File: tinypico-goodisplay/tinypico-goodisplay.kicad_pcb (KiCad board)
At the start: 2 copper layers, 53.8 x 17.8 mm, 34 parts, among them J1 AFC24-S24FIC-00, Q1 Si1308, U1 TinypicoESP32_Symbol, U2 PCF8563T, Y1 Crystal_Small

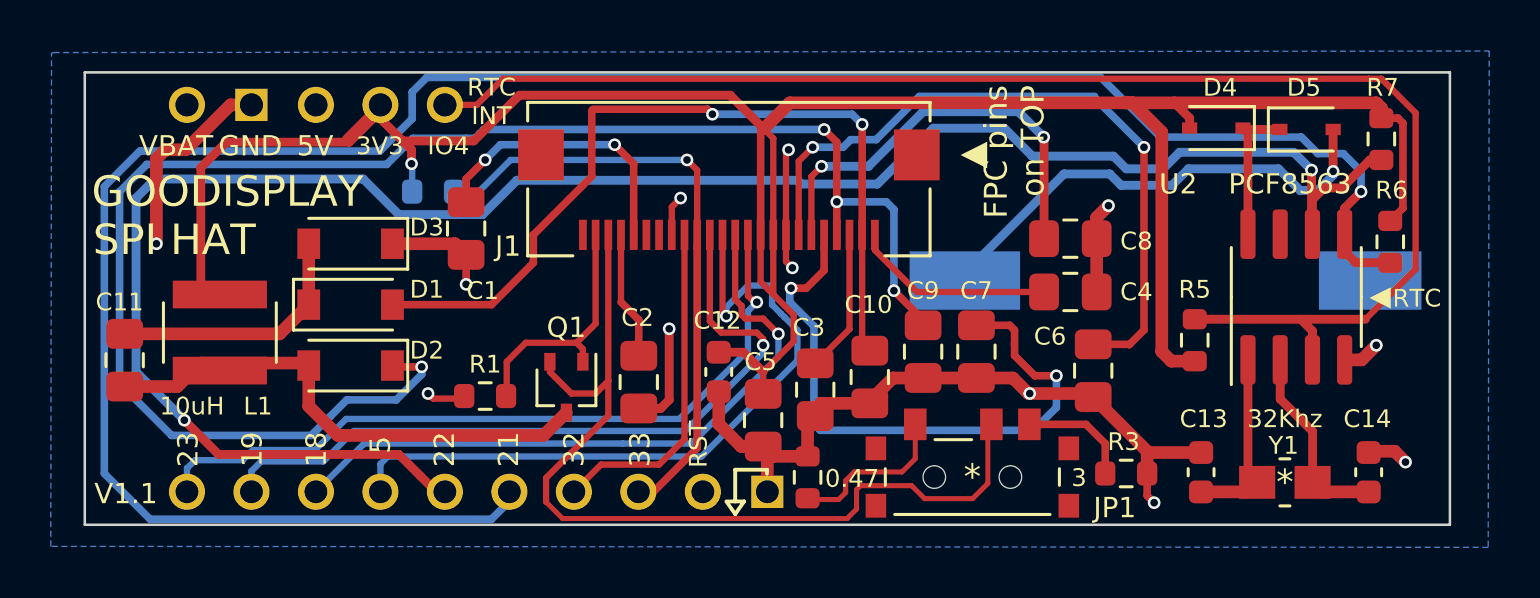
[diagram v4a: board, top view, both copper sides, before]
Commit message: Relabeling Sylkscreen with SPI pins
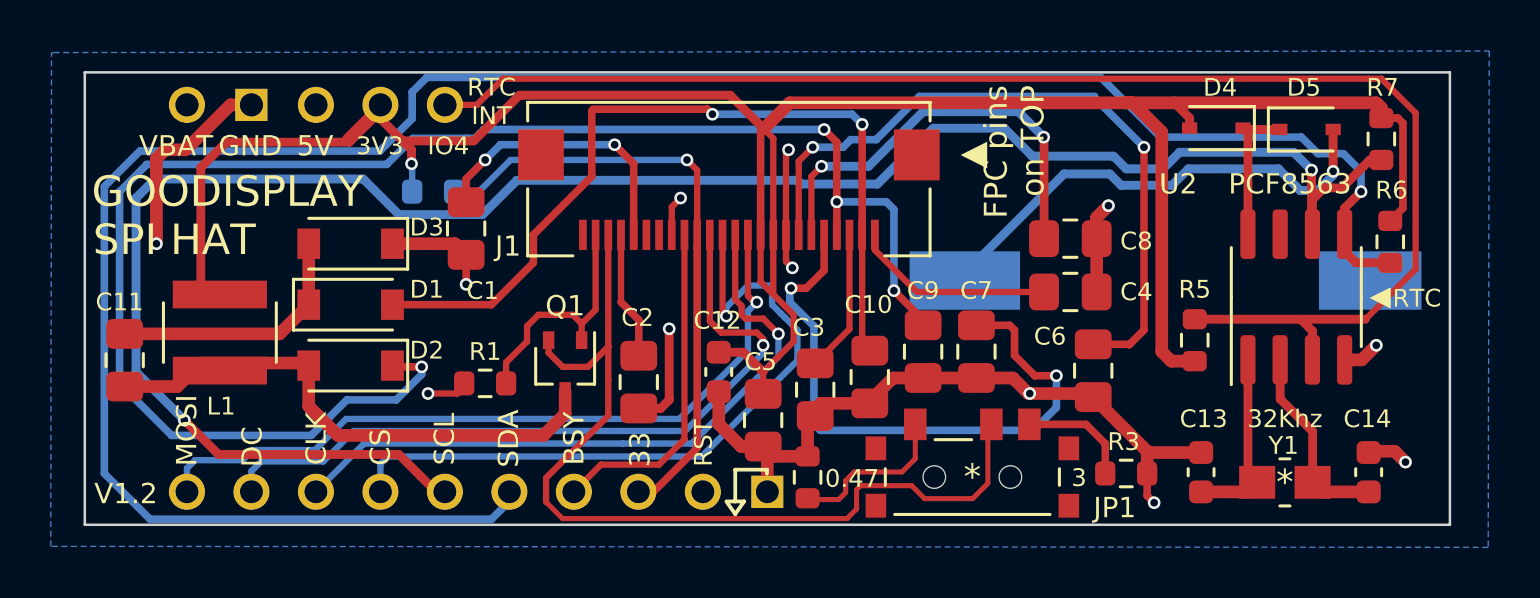
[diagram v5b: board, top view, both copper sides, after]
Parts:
- moved Q1 0.85 mm to (91.2, 46.4)
- moved R1 0.50 mm to (88.0, 47.0)
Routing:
- net Net-(C11-Pad2): track 20.3 -> 21.1 mm
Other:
- board text added: "BSY"
- board text added: "CLK"
- board text added: "CS"
- board text added: "DC"
- board text added: "MOSI"
- board text added: "SCL"
- board text added: "SDA"
- board text added: "V1.2"
- board text removed: "18"
- board text removed: "19"
- board text removed: "21"
- board text removed: "22"
- board text removed: "23"
- board text removed: "32"
- board text removed: "5"
- board text removed: "V1.1"
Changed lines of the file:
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@@
   )
   (footprint "Package_TO_SOT_SMD:SOT-323_SC-70" (layer "F.Cu")
-    (at 91.2 47.2 -90)
+    (at 91.15 46.35 -90)
     (descr "SOT-323, SC-70")
     (tags "SOT-323 SC-70")
@@
     (property "Sheetname" "")
     (attr through_hole)
-    (fp_text reference "L1" (at -2.9 1.5 180) (layer "F.SilkS")
-      (effects (font (size 0.7 0.7) (thickness 0.13)))
-    )
-    (fp_text value "10uH" (at -2.9 -1.1 180) (layer "F.SilkS")
+    (fp_text reference "L1" (at -2.9 0.05 180) (layer "F.SilkS")
+      (effects (font (size 0.7 0.7) (thickness 0.13)))
+    )
+    (fp_text value "10uH" (at -2.9 -1.1 180) (layer "F.SilkS") hide
       (effects (font (size 0.7 0.7) (thickness 0.13)))
     )
@@
   )
   (footprint "Resistor_SMD:R_0603_1608Metric" (layer "F.Cu")
-    (at 88 47.55 180)
+    (at 88 47.05 180)
     (descr "Resistor SMD 0603 (1608 Metric), square (rectangular) end terminal, IPC_7351 nominal, (Body size source: IPC-SM-782 page 72, https://www.pcb-3d.com/wordpress/wp-content/uploads/ipc-sm-782a_amendment_1_and_2.pdf), generated with kicad-footprint-generator")
     (tags "resistor")
@@
     (effects (font (size 1.2 1.2) (thickness 0.2)) (justify left))
   )
-  (gr_text "32" (at 91.5 49.65 90) (layer "F.SilkS")
+  (gr_text "BSY" (at 91.5 49.22381 90) (layer "F.SilkS")
     (effects (font (size 0.8 0.8) (thickness 0.12)))
   )
-  (gr_text "18" (at 81.35 49.65 90) (layer "F.SilkS")
+  (gr_text "CLK" (at 81.35 49.22381 90) (layer "F.SilkS")
     (effects (font (size 0.8 0.8) (thickness 0.12)))
   )
-  (gr_text "23" (at 76.3 49.65 90) (layer "F.SilkS")
+  (gr_text "MOSI" (at 76.25 48.9 90) (layer "F.SilkS")
     (effects (font (size 0.8 0.8) (thickness 0.12)))
   )
@@
     (effects (font (size 0.8 0.8) (thickness 0.12)))
   )
-  (gr_text "19" (at 78.825 49.65 90) (layer "F.SilkS")
+  (gr_text "DC" (at 78.825 49.547619 90) (layer "F.SilkS")
     (effects (font (size 0.8 0.8) (thickness 0.12)))
   )
-  (gr_text "22" (at 86.4 49.65 90) (layer "F.SilkS")
+  (gr_text "SCL" (at 86.4 49.242857 90) (layer "F.SilkS")
     (effects (font (size 0.8 0.8) (thickness 0.12)))
   )
-  (gr_text "5" (at 83.875 49.475001 90) (layer "F.SilkS")
+  (gr_text "CS" (at 83.875 49.566667 90) (layer "F.SilkS")
     (effects (font (size 0.8 0.8) (thickness 0.12)))
   )
-  (gr_text "21" (at 88.925 49.65 90) (layer "F.SilkS")
+  (gr_text "SDA" (at 88.925 49.22381 90) (layer "F.SilkS")
     (effects (font (size 0.8 0.8) (thickness 0.12)))
   )
@@
     (effects (font (size 0.8 0.8) (thickness 0.12)))
   )
-  (gr_text "V1.1" (at 73.85 51.4) (layer "F.SilkS")
+  (gr_text "V1.2" (at 73.85 51.4) (layer "F.SilkS")
     (effects (font (size 0.8 0.8) (thickness 0.12)))
   )
@@
     (effects (font (size 0.8 0.8) (thickness 0.12)))
   )
-  (gr_text "RST" (at 96.4 49.45 90) (layer "F.SilkS")
+  (gr_text "RST" (at 96.6 49.4 90) (layer "F.SilkS")
     (effects (font (size 0.7 0.7) (thickness 0.12)))
   )
@@
   (segment (start 97.2 47.375) (end 97.2 48.65) (width 0.5) (layer "F.Cu") (net 2))
   (segment (start 112.0875 43.45) (end 112.0875 41.35) (width 0.5) (layer "F.Cu") (net 2))
+  (segment (start 87.175 47.05) (end 87.175 47.175) (width 0.25) (layer "F.Cu") (net 2))
   (segment (start 112.0875 40.5125) (end 112.55 40.05) (width 0.5) (layer "F.Cu") (net 2))
   (segment (start 101 48.05) (end 101.2125 47.8375) (width 0.5) (layer "F.Cu") (net 2))
@@
   (segment (start 101.2125 47.8375) (end 103.15 47.8375) (width 0.5) (layer "F.Cu") (net 2))
   (segment (start 103.15 47.75) (end 104.0625 46.8375) (width 0.5) (layer "F.Cu") (net 2))
+  (segment (start 86.9 47.45) (end 85.75 47.45) (width 0.25) (layer "F.Cu") (net 2))
   (segment (start 99.114 51.32) (end 99.114 49.7015) (width 0.5) (layer "F.Cu") (net 2))
   (segment (start 100.7 49.925) (end 99.3375 49.925) (width 0.5) (layer "F.Cu") (net 2))
@@
   (segment (start 77.97 36.08) (end 76.2 37.85) (width 0.5) (layer "F.Cu") (net 2))
   (segment (start 97.2 48.65) (end 98.0875 49.5375) (width 0.5) (layer "F.Cu") (net 2))
-  (segment (start 85.95 47.65) (end 85.75 47.45) (width 0.25) (layer "F.Cu") (net 2))
   (segment (start 122.525 46.125) (end 123.1 45.55) (width 0.5) (layer "F.Cu") (net 2))
   (segment (start 111.8 47.45) (end 111.95 47.6) (width 0.5) (layer "F.Cu") (net 2))
@@
   (segment (start 84.35 41.55) (end 86.8125 41.55) (width 0.5) (layer "F.Cu") (net 2))
   (segment (start 94.9125 48.0375) (end 95.25 47.7) (width 0.35) (layer "F.Cu") (net 2))
-  (segment (start 86.85 47.65) (end 85.95 47.65) (width 0.25) (layer "F.Cu") (net 2))
   (segment (start 100.7 49.925) (end 100.7 48.6375) (width 0.5) (layer "F.Cu") (net 2))
   (segment (start 103.15 47.8375) (end 103.15 47.75) (width 0.5) (layer "F.Cu") (net 2))
   (segment (start 121.855 46.125) (end 122.525 46.125) (width 0.5) (layer "F.Cu") (net 2))
+  (segment (start 87.175 47.175) (end 86.9 47.45) (width 0.25) (layer "F.Cu") (net 2))
   (segment (start 101 48.3375) (end 101 48.05) (width 0.5) (layer "F.Cu") (net 2))
   (segment (start 111.95 47.6) (end 114.075 49.725) (width 0.5) (layer "F.Cu") (net 2))
@@
   (segment (start 79.9 45.1) (end 81.05 43.95) (width 0.5) (layer "F.Cu") (net 25))
   (segment (start 90.3 49.1) (end 82.2 49.1) (width 0.5) (layer "F.Cu") (net 26))
+  (segment (start 91.15 48.25) (end 91.15 47.35) (width 0.5) (layer "F.Cu") (net 26))
   (segment (start 75.875 47.175) (end 76.8 46.25) (width 0.5) (layer "F.Cu") (net 26))
-  (segment (start 91.2 48.2) (end 90.3 49.1) (width 0.5) (layer "F.Cu") (net 26))
   (segment (start 80.95 46.25) (end 81.05 46.35) (width 0.5) (layer "F.Cu") (net 26))
   (segment (start 76.8 46.25) (end 80.95 46.25) (width 0.5) (layer "F.Cu") (net 26))
@@
   (segment (start 73.8 47.175) (end 75.875 47.175) (width 0.5) (layer "F.Cu") (net 26))
   (segment (start 82.2 49.1) (end 81.05 47.95) (width 0.5) (layer "F.Cu") (net 26))
+  (segment (start 90.3 49.1) (end 91.15 48.25) (width 0.5) (layer "F.Cu") (net 26))
   (segment (start 90.4 51.725) (end 91.05 52.375) (width 0.2) (layer "F.Cu") (net 29))
-  (segment (start 92.849999 41.199999) (end 92.85 46.95) (width 0.25) (layer "F.Cu") (net 29))
+  (segment (start 91.05 46.4) (end 90.5 45.85) (width 0.25) (layer "F.Cu") (net 29))
   (segment (start 90.4 50.775) (end 90.4 51.725) (width 0.25) (layer "F.Cu") (net 29))
+  (segment (start 92.05 46.4) (end 91.05 46.4) (width 0.25) (layer "F.Cu") (net 29))
   (segment (start 102.255 52.375) (end 102.63 52) (width 0.2) (layer "F.Cu") (net 29))
   (segment (start 92.85 48.325) (end 90.4 50.775) (width 0.25) (layer "F.Cu") (net 29))
   (segment (start 107.8 50.99) (end 107.8 48.80412) (width 0.2) (layer "F.Cu") (net 29))
   (segment (start 92.85 46.95) (end 92.85 48.325) (width 0.25) (layer "F.Cu") (net 29))
-  (segment (start 92.35 47.45) (end 92.85 46.95) (width 0.25) (layer "F.Cu") (net 29))
   (segment (start 105.31 51.59) (end 107.2 51.59) (width 0.2) (layer "F.Cu") (net 29))
-  (segment (start 90.55 46.2) (end 90.55 46.6) (width 0.25) (layer "F.Cu") (net 29))
   (segment (start 102.63 51.23) (end 102.78 51.08) (width 0.2) (layer "F.Cu") (net 29))
-  (segment (start 91.4 47.45) (end 92.35 47.45) (width 0.25) (layer "F.Cu") (net 29))
-  (segment (start 90.55 46.6) (end 91.4 47.45) (width 0.25) (layer "F.Cu") (net 29))
+  (segment (start 90.5 45.85) (end 90.5 45.35) (width 0.25) (layer "F.Cu") (net 29))
+  (segment (start 92.85 45.6) (end 92.85 46.95) (width 0.25) (layer "F.Cu") (net 29))
   (segment (start 102.78 51.08) (end 104.8 51.08) (width 0.2) (layer "F.Cu") (net 29))
+  (segment (start 92.85 45.6) (end 92.05 46.4) (width 0.25) (layer "F.Cu") (net 29))
   (segment (start 107.8 48.80412) (end 107.9393 48.66482) (width 0.2) (layer "F.Cu") (net 29))
   (segment (start 102.63 52) (end 102.63 51.23) (width 0.2) (layer "F.Cu") (net 29))
   (segment (start 91.05 52.375) (end 102.255 52.375) (width 0.2) (layer "F.Cu") (net 29))
+  (segment (start 92.849999 41.199999) (end 92.85 45.6) (width 0.25) (layer "F.Cu") (net 29))
   (segment (start 104.8 51.08) (end 105.31 51.59) (width 0.2) (layer "F.Cu") (net 29))
   (segment (start 107.2 51.59) (end 107.8 50.99) (width 0.2) (layer "F.Cu") (net 29))
-  (segment (start 88.85 46.2) (end 88.85 47.65) (width 0.25) (layer "F.Cu") (net 30))
-  (segment (start 91.6 45.45) (end 89.6 45.45) (width 0.25) (layer "F.Cu") (net 30))
-  (segment (start 92.35 44.7) (end 91.6 45.45) (width 0.25) (layer "F.Cu") (net 30))
-  (segment (start 92.35 41.199999) (end 92.35 44.7) (width 0.25) (layer "F.Cu") (net 30))
-  (segment (start 91.85 45.7) (end 91.6 45.45) (width 0.25) (layer "F.Cu") (net 30))
-  (segment (start 89.6 45.45) (end 88.85 46.2) (width 0.25) (layer "F.Cu") (net 30))
-  (segment (start 91.85 46.2) (end 91.85 45.7) (width 0.25) (layer "F.Cu") (net 30))
+  (segment (start 89.65 44.8) (end 90.1 44.35) (width 0.25) (layer "F.Cu") (net 30))
+  (segment (start 89.65 45.4) (end 89.65 44.8) (width 0.25) (layer "F.Cu") (net 30))
+  (segment (start 88.825 46.225) (end 89.65 45.4) (width 0.25) (layer "F.Cu") (net 30))
+  (segment (start 92.35 44.15) (end 91.8 44.7) (width 0.25) (layer "F.Cu") (net 30))
+  (segment (start 91.45 44.35) (end 91.8 44.7) (width 0.25) (layer "F.Cu") (net 30))
+  (segment (start 92.35 41.199999) (end 92.35 44.15) (width 0.25) (layer "F.Cu") (net 30))
+  (segment (start 91.8 44.7) (end 91.8 45.35) (width 0.25) (layer "F.Cu") (net 30))
+  (segment (start 90.1 44.35) (end 91.45 44.35) (width 0.25) (layer "F.Cu") (net 30))
+  (segment (start 88.825 47.05) (end 88.825 46.225) (width 0.25) (layer "F.Cu") (net 30))
   (segment (start 120.5922 48.9422) (end 120.5922 50.95) (width 0.35) (layer "F.Cu") (net 32))
   (segment (start 122.8 51.325) (end 120.9672 51.325) (width 0.5) (layer "F.Cu") (net 32))

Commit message: Update several production files (Tiny GOODISPLAY)
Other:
- board text added: "6 EPD_RST"
- board text added: "7 BUSY"
- board text added: "8 SDA"
- board text added: "9 SCL"
- board text removed: "6"
- board text removed: "7"
- board text removed: "8"
- board text removed: "9"
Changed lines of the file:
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@@
   (gr_line (start 126 34.8) (end 72.23 34.8) (layer "Edge.Cuts") (width 0.1))
   (gr_line (start 126 52.62) (end 126 34.8) (layer "Edge.Cuts") (width 0.1))
-  (gr_text "6" (at 93.985978 49.878571 270) (layer "B.SilkS")
+  (gr_text "6 EPD_RST" (at 93.985978 46.664286 270) (layer "B.SilkS")
     (effects (font (size 0.9 0.9) (thickness 0.13)) (justify mirror))
   )
@@
     (effects (font (size 0.9 0.9) (thickness 0.13)) (justify mirror))
   )
-  (gr_text "8" (at 88.90427 49.878571 270) (layer "B.SilkS")
+  (gr_text "8 SDA" (at 88.90427 48.271428 270) (layer "B.SilkS")
     (effects (font (size 0.9 0.9) (thickness 0.13)) (justify mirror))
   )
@@
     (effects (font (size 1.4 1.4) (thickness 0.3)) (justify mirror))
   )
-  (gr_text "7" (at 91.445124 49.878571 270) (layer "B.SilkS")
+  (gr_text "7 BUSY" (at 91.445124 47.8 270) (layer "B.SilkS")
     (effects (font (size 0.9 0.9) (thickness 0.13)) (justify mirror))
   )
@@
     (effects (font (size 0.8 0.8) (thickness 0.14)) (justify mirror))
   )
-  (gr_text "9" (at 86.363416 49.878571 270) (layer "B.SilkS")
+  (gr_text "9 SCL" (at 86.363416 48.292857 270) (layer "B.SilkS")
     (effects (font (size 0.9 0.9) (thickness 0.13)) (justify mirror))
   )
